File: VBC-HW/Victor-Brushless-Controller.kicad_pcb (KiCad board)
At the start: 2 copper layers, 85 parts, among them J1 i2c QWIIC, P1 PVDD, P2 GND, Q1 TPH4R008NH, Q2 TPH4R008NH, Q3 TPH4R008NH, Q4 TPH4R008NH, Q5 TPH4R008NH, Q6 TPH4R008NH, SW1 SW_SPST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

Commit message: Preliminary component placing
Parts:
- J1: value i2c QWIIC -> i2c/UART; moved to B.Cu
- JP1: value SolderJumper -> 3V3
- P1: value PVDD -> V+
- PA1: value Phase -> A
- PB1: value Phase -> B; moved to B.Cu
- PC1: value Phase -> C
- SW1: value SW_SPST -> BOOT
- SW2: value SW_SPST -> RESET
- U6: value External SPI -> SPI; moved to B.Cu
- U7: moved to B.Cu
- moved C31 113.7 mm to (191.2, 102.0), turned to 90 degrees
- moved C26 113.7 mm to (191.2, 97.0), turned to 90 degrees
- moved PC1 106.4 mm to (192.8, 114.2)
- moved D2 105.7 mm to (194.0, 99.5), turned to 90 degrees
- moved JP1 104.9 mm to (169.7, 74.5)
- moved U2 104.8 mm to (185.0, 81.8)
- moved U5 101.1 mm to (199.5, 106.0), turned to 90 degrees
- moved R1 98.2 mm to (188.0, 101.0), turned to 90 degrees
- moved D1 96.8 mm to (164.5, 76.5), turned to -90 degrees
- moved Q1 95.4 mm to (166.0, 110.0), turned to 180 degrees
- moved PB1 94.7 mm to (177.0, 114.2), turned to 180 degrees
- moved Q2 94.4 mm to (171.5, 108.6)
- moved C30 93.6 mm to (197.0, 107.0), turned to 90 degrees
- moved Q3 93.6 mm to (177.0, 108.6)
- moved R2 93.6 mm to (183.5, 101.0), turned to -90 degrees
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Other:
- board outline added: 44 x 44 mm

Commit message: PCB starting to take shape
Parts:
- D1: value B230A-13-F -> SMA_L4.4-W2.6-LS5.0-RD
- moved C13 61.4 mm to (200.0, 94.2), turned to -90 degrees
- moved R10 57.0 mm to (198.5, 94.0), turned to -90 degrees
- moved R9 56.1 mm to (197.0, 94.0), turned to 90 degrees
- moved R11 53.5 mm to (195.5, 94.0), turned to -90 degrees
- moved C10 10.4 mm to (131.5, 108.5)
- moved LED1 1.80 mm to (153.0, 89.5)
- moved P2 1.50 mm to (198.5, 98.0)
- moved D2 1.00 mm to (194.0, 100.5)
- moved P1 1.00 mm to (198.5, 103.0)
- moved U5 1.00 mm to (199.5, 107.0)
- moved C4 0.50 mm to (158.5, 98.5)
- moved H1 0.50 mm to (197.0, 91.0)
- moved H2 0.50 mm to (197.0, 80.7)
- moved H3 0.50 mm to (199.5, 80.7)

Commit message: Updated PCB and code
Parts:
- C24, C32, C33, C34, C35, C36, C37, C38, C39: moved to B.Cu
- LED1: value Red -> nFault
- LED2: value Blue -> VD
- LED3: value Yellow -> IO15
- moved C38 61.8 mm to (194.2, 98.0), turned to -90 degrees
- moved C37 60.1 mm to (191.2, 98.0), turned to -90 degrees
- moved C36 58.1 mm to (194.0, 103.0), turned to -90 degrees
- moved C39 55.5 mm to (191.5, 103.0), turned to -90 degrees
- moved C24 53.3 mm to (179.2, 103.0), turned to 90 degrees
- moved LED2 50.9 mm to (193.2, 92.0)
- moved R8 49.4 mm to (189.5, 93.2)
- moved R15 49.0 mm to (193.2, 94.2)
- moved C27 48.0 mm to (178.5, 102.5), turned to 90 degrees
- moved C20 47.6 mm to (172.2, 81.8)
- moved C23 47.2 mm to (173.0, 102.5), turned to 90 degrees
- moved R4 46.7 mm to (183.5, 93.2)
- moved C25 46.5 mm to (175.8, 102.5), turned to 90 degrees
- moved C32 46.0 mm to (177.0, 103.0), turned to 90 degrees
- moved C22 44.9 mm to (170.2, 102.5), turned to 90 degrees
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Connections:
- U2 pad 23: IO15 -> IO 15

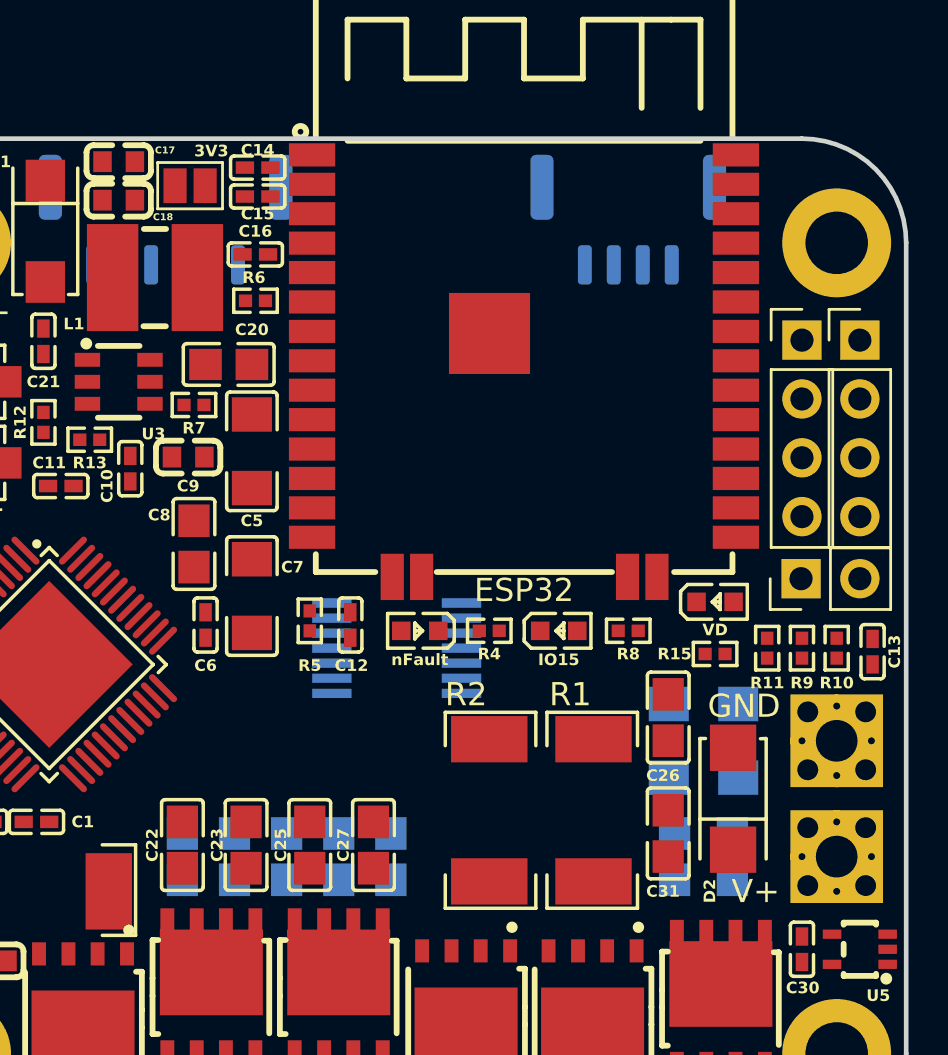
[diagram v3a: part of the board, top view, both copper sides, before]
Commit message: Updates connections in board
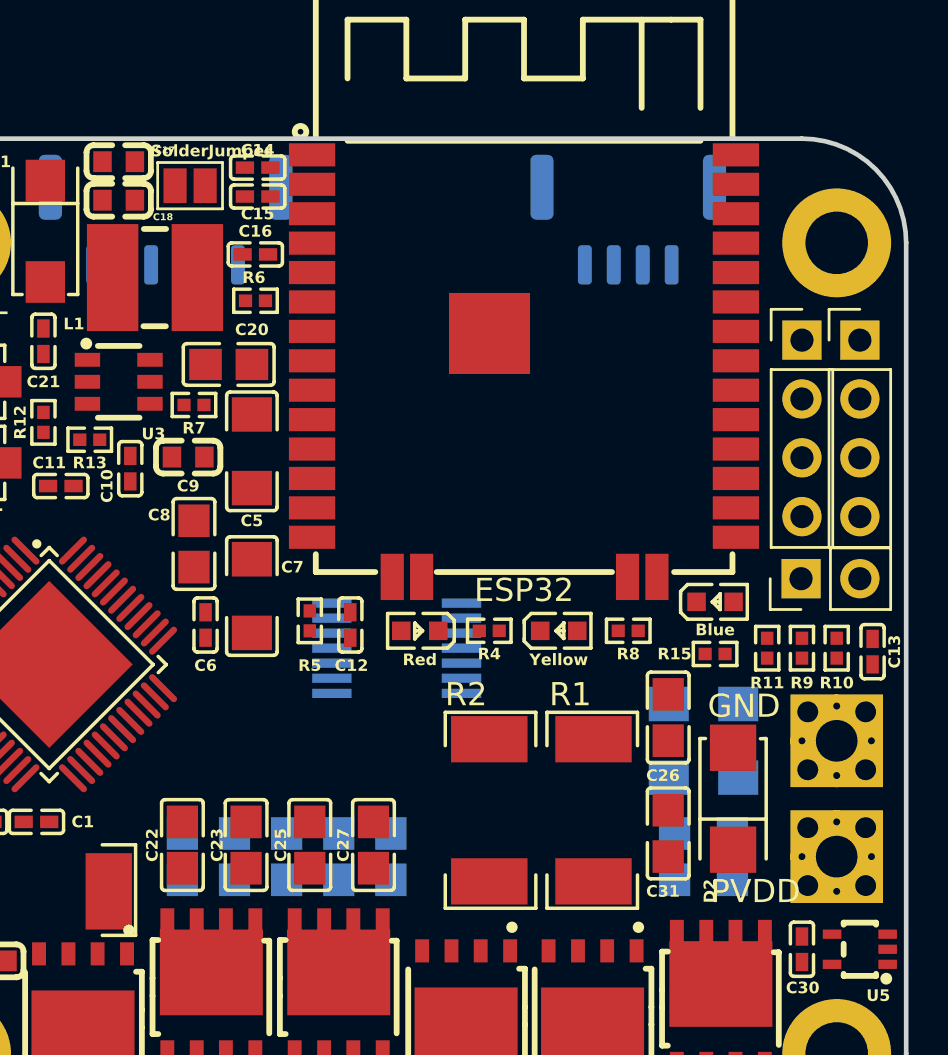
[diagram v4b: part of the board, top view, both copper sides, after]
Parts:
- D1: value SMA_L4.4-W2.6-LS5.0-RD -> B230A-13-F
- J1: value i2c/UART -> i2c QWIIC
- JP1: value 3V3 -> SolderJumper
- LED1: value nFault -> Red
- LED2: value VD -> Blue
- LED3: value IO15 -> Yellow
- P1: value V+ -> PVDD
- U6: value SPI -> External SPI
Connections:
- net IO 15 renamed IO15
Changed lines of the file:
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@@
 	(net 26 "Net-(LED1-K)")
 	(net 27 "Net-(LED2-A)")
-	(net 28 "IO 15")
+	(net 28 "IO15")
 	(net 29 "Net-(LED3-K)")
 	(net 30 "/PA")
@@
 			)
 		)
-		(property "Value" "IO15"
+		(property "Value" "Yellow"
 			(at 0 1.25 0)
 			(layer "F.SilkS")
@@
 			(size 0.8 0.8)
 			(layers "F.Cu" "F.Paste" "F.Mask")
-			(net 28 "IO 15")
+			(net 28 "IO15")
 			(pinfunction "A")
 			(pintype "passive")
@@
 		(at 178.5 102.5 90)
 		(property "Reference" "C27"
-			(at 0 -1.3 270)
+			(at 0 -1.3 -90)
 			(layer "F.SilkS")
 			(effects
@@
 		)
 		(property "Value" "10uF"
-			(at 0 4 270)
+			(at 0 4 -90)
 			(layer "F.Fab")
 			(hide yes)
@@
 			)
 		)
+		(property ki_fp_filters "C_*")
+		(sheetname "Root")
+		(sheetfile "Victor-Brushless-Controller.kicad_sch")
 		(attr smd)
 		(fp_line
@@
 		(at 173 102.5 90)
 		(property "Reference" "C23"
-			(at 0 -1.25 270)
+			(at 0 -1.25 -90)
 			(layer "F.SilkS")
 			(effects
@@
 		)
 		(property "Value" "10uF"
-			(at 0 4 270)
+			(at 0 4 -90)
 			(layer "F.Fab")
 			(hide yes)
@@
 			)
 		)
-		(property "Value" "nFault"
+		(property "Value" "Red"
 			(at 0 -1.25 180)
 			(layer "F.SilkS")
@@
 		(at 175.75 102.5 90)
 		(property "Reference" "C25"
-			(at 0 -1.25 270)
+			(at 0 -1.25 -90)
 			(layer "F.SilkS")
 			(effects
@@
 		)
 		(property "Value" "10uF"
-			(at 0 4 270)
+			(at 0 4 -90)
 			(layer "F.Fab")
 			(hide yes)
@@
 			)
 		)
-		(property "Value" "VD"
+		(property "Value" "Blue"
 			(at 0 1.21 0)
 			(layer "F.SilkS")
@@
 			)
 		)
+		(sheetname "Root")
+		(sheetfile "Victor-Brushless-Controller.kicad_sch")
 		(attr smd)
 		(fp_line
@@
 			)
 		)
-		(property "Value" "3V3"
+		(property "Value" "SolderJumper"
 			(at 0.917764 -1.5 0)
 			(layer "F.SilkS")
@@
 			)
 		)
-		(property "Value" "SMA_L4.4-W2.6-LS5.0-RD"
+		(property "Value" "B230A-13-F"
 			(at 0 4 -90)
 			(layer "F.Fab")
@@
 			)
 		)
+		(sheetname "Root")
+		(sheetfile "Victor-Brushless-Controller.kicad_sch")
 		(attr smd)
 		(fp_line
@@
 			)
 		)
-		(property "Value" "V+"
+		(property "Value" "PVDD"
 			(at -3.5 1.5 0)
 			(unlocked yes)
@@
 			)
 		)
+		(sheetname "Root")
+		(sheetfile "Victor-Brushless-Controller.kicad_sch")
 		(attr smd)
 		(fp_line
@@
 			)
 		)
+		(property ki_fp_filters "C_*")
+		(sheetname "Root")
+		(sheetfile "Victor-Brushless-Controller.kicad_sch")
 		(attr smd)
 		(fp_line
@@
 		(at 170.25 102.5 90)
 		(property "Reference" "C22"
-			(at 0 -1.3 270)
+			(at 0 -1.3 -90)
 			(layer "F.SilkS")
 			(effects
@@
 		)
 		(property "Value" "10uF"
-			(at 0 4 270)
+			(at 0 4 -90)
 			(layer "F.Fab")
 			(hide yes)
@@
 			)
 		)
+		(sheetname "Root")
+		(sheetfile "Victor-Brushless-Controller.kicad_sch")
 		(attr smd)
 		(fp_line
@@
 			)
 		)
+		(property ki_fp_filters "Choke_* *Coil* Inductor_* L_*")
+		(sheetname "Root")
+		(sheetfile "Victor-Brushless-Controller.kicad_sch")
 		(attr smd)
 		(fp_line
@@
 			)
 		)
+		(property ki_fp_filters "C_*")
+		(sheetname "Root")
+		(sheetfile "Victor-Brushless-Controller.kicad_sch")
 		(attr smd)
 		(fp_line
@@
 			)
 		)
+		(sheetname "Root")
+		(sheetfile "Victor-Brushless-Controller.kicad_sch")
 		(attr smd)
 		(fp_line
@@
 			(size 2 1)
 			(layers "F.Cu" "F.Paste" "F.Mask")
-			(net 28 "IO 15")
+			(net 28 "IO15")
 			(pinfunction "IO15")
 			(pintype "unspecified")
@@
 			)
 		)
+		(sheetname "Root")
+		(sheetfile "Victor-Brushless-Controller.kicad_sch")
 		(attr smd)
 		(fp_line
@@
 		)
 		(property "Value" "10uF"
-			(at 0 -4 270)
+			(at 0 -4 -90)
 			(layer "B.Fab")
 			(hide yes)
@@
 		)
 		(property "Value" "10uF"
-			(at 0 -4 270)
+			(at 0 -4 -90)
 			(layer "B.Fab")
 			(hide yes)
@@
 		)
 		(property "Value" "10uF"
-			(at 0 -4 270)
+			(at 0 -4 -90)
 			(layer "B.Fab")
 			(hide yes)
@@
 			)
 		)
-		(property "Value" "SPI"
+		(property "Value" "External SPI"
 			(at -6.975 0.5 180)
 			(layer "B.SilkS")
@@
 			)
 		)
-		(property "Value" "i2c/UART"
+		(property "Value" "i2c QWIIC"
 			(at 6.5 0.5 180)
 			(layer "B.SilkS")
@@
 		)
 		(property "Value" "10uF"
-			(at 0 -4 270)
+			(at 0 -4 -90)
 			(layer "B.Fab")
 			(hide yes)
@@
 		)
 		(property "Value" "10uF"
-			(at 0 -4 270)
+			(at 0 -4 -90)
 			(layer "B.Fab")
 			(hide yes)

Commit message: Starting added traces to board
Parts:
- removed REF**: MountingHole_2.7mm_M2.5_DIN965_Pad, MountingHole:MountingHole_2.7mm_M2.5_DIN965_Pad
- added ?: , , F.Cu at (160.5, 111.5)
- JP1: value SolderJumper -> 3V3
- P1: value PVDD -> V+
- moved Q6 27.5 mm to (166.0, 110.0), turned to 180 degrees
- moved PA1 22.2 mm to (193.0, 114.5)
- moved PC1 22.2 mm to (170.8, 114.5)
- moved Q1 21.9 mm to (187.9, 109.9)
- moved Q2 21.9 mm to (193.4, 108.9)
- moved Q5 16.5 mm to (171.5, 108.9), turned to 0 degrees
- moved C16 2.25 mm to (173.4, 79.2)
- moved C10 1.98 mm to (167.3, 88.1), turned to 0 degrees
- moved C6 1.80 mm to (171.2, 94.8), turned to -90 degrees
- moved R6 1.75 mm to (173.4, 77.2)
- moved C8 1.23 mm to (171.0, 90.7)
- moved C11 1.17 mm to (164.6, 88.1), turned to 180 degrees
- moved C9 1.09 mm to (170.2, 86.8)
- moved C4 0.92 mm to (158.3, 97.6), turned to -90 degrees
- moved R7 0.90 mm to (170.8, 84.4)
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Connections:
- H2 pad 1: BOOT IO0 -> TX0
- H2 pad 2: RESET EN -> RX0
- H2 pad 3: RX0 -> RESET EN
- H2 pad 4: TX0 -> BOOT IO0
- U2 pad 39: unconnected-(U2-P_GND-Pad39) -> GND
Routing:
- net GND: track 0.00 -> 76.5 mm
- net /GHB: track 0.00 -> 25.6 mm
- net IO22: track 0.00 -> 22.5 mm
- net IO21: track 0.00 -> 21.2 mm
- net /GHC: track 0.00 -> 20.2 mm
- net VCC: track 0.00 -> 17.8 mm
- net /PC: track 0.00 -> 14.9 mm
- net /SLC: track 0.00 -> 10.9 mm
- net /GLC: track 0.00 -> 8.91 mm
- net 3V3A: track 0.00 -> 8.29 mm
- net Net-(U1-VDRAIN): track 0.00 -> 8.20 mm
- net RESET EN: track 0.00 -> 6.91 mm
- net Net-(U1-CP1L): track 0.00 -> 6.69 mm
- net Net-(U1-CP1H): track 0.00 -> 5.67 mm
- net BOOT IO0: track 0.00 -> 5.63 mm
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
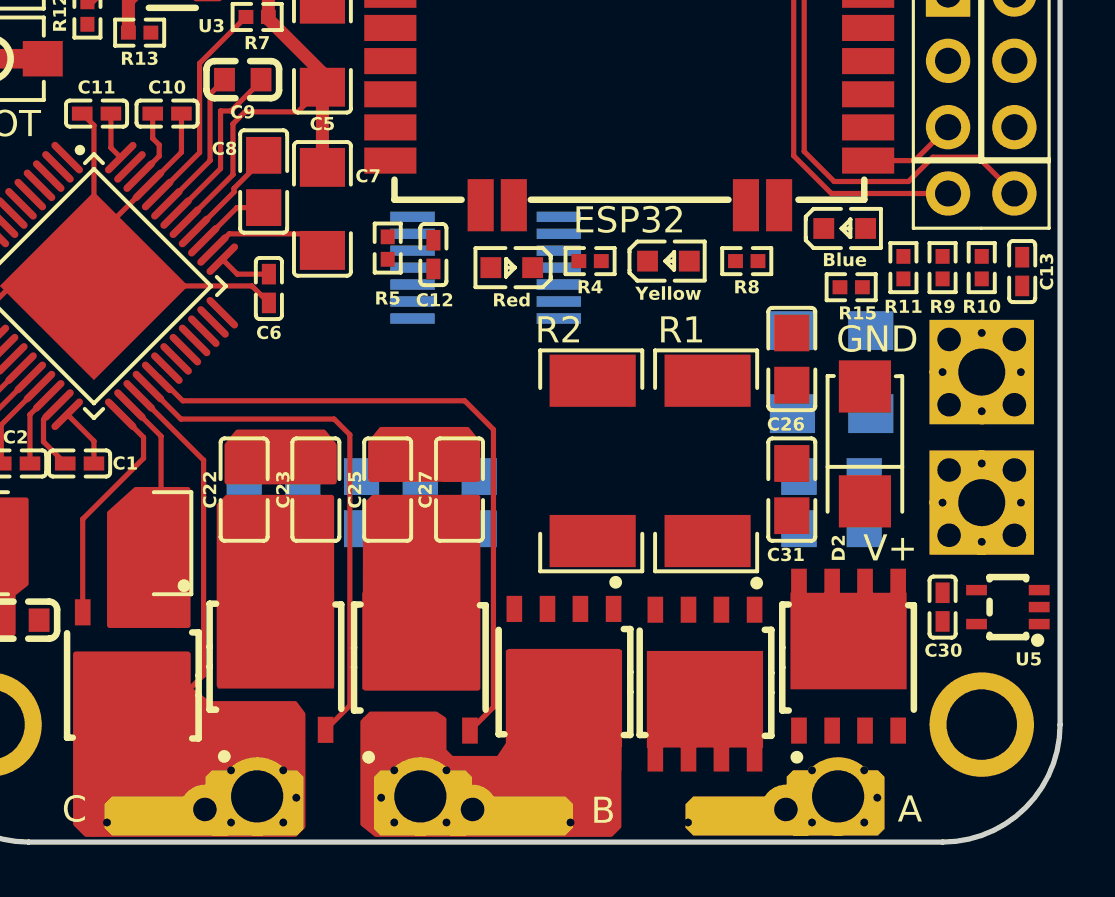
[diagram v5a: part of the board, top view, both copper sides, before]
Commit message: Finished top layer connections
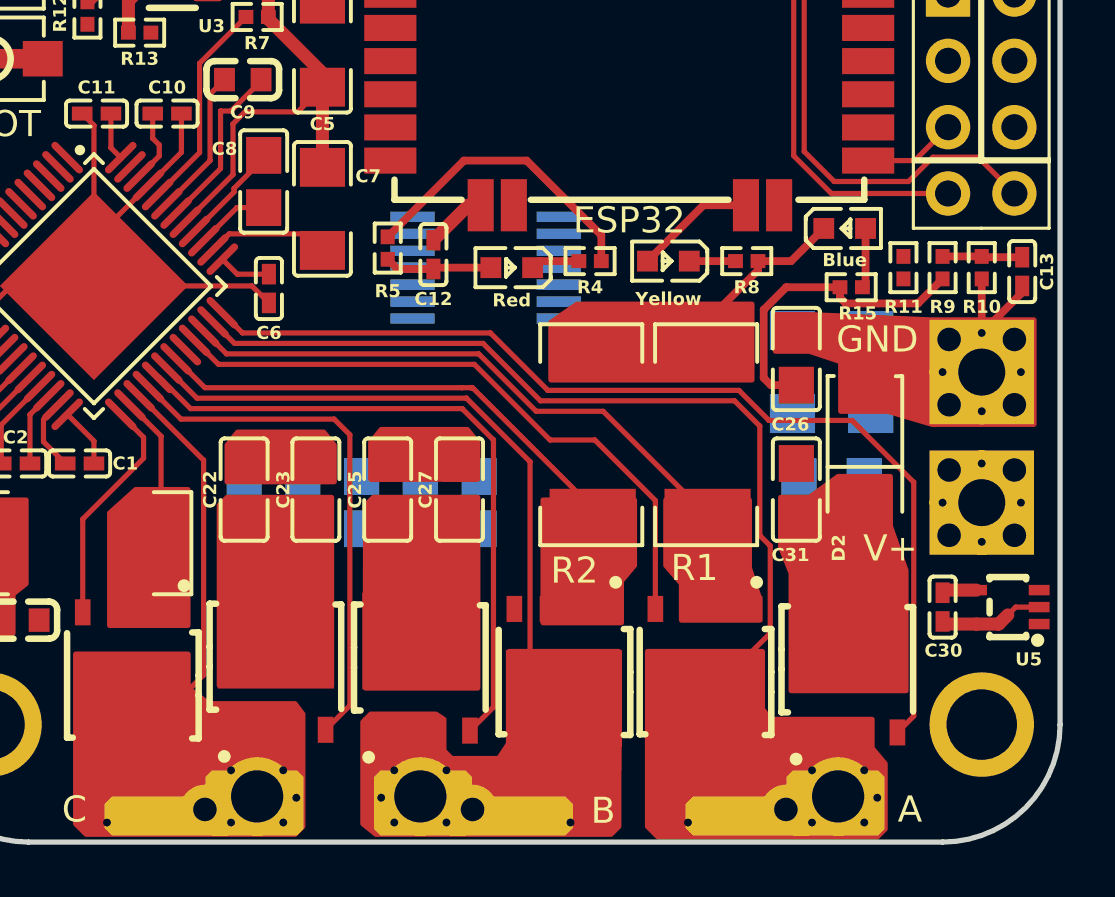
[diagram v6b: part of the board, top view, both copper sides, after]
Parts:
- moved Q2 5.58 mm to (187.9, 109.9), turned to 180 degrees
- moved Q1 5.54 mm to (193.4, 109.0), turned to 0 degrees
- moved R1 1.00 mm to (188.0, 100.4)
- moved R2 1.00 mm to (183.6, 100.4)
- moved C26 0.17 mm to (191.4, 97.5)
- moved C31 0.17 mm to (191.4, 102.5)
- turned C12 to -90 degrees
- turned LED3 to 180 degrees
- turned R5 to 90 degrees
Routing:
- net /GHA: track 0.00 -> 39.0 mm
- net /PA: track 0.00 -> 34.2 mm
- net /PB: track 0.00 -> 25.0 mm
- net /GLA: track 0.00 -> 24.3 mm
- net /SLA: track 2.81 -> 25.4 mm
- net /SLB: track 3.55 -> 23.1 mm
- net GND: track 76.5 -> 94.8 mm
- net VCC: track 17.8 -> 29.9 mm
- net nFault IO4: track 0.00 -> 11.6 mm
- net 3V3A: track 8.29 -> 13.8 mm
- net IO15: track 0.00 -> 4.66 mm
- net Vbus IO33: track 0.00 -> 3.06 mm
- net Net-(LED2-A): track 0.00 -> 2.30 mm
- net Net-(LED1-K): track 0.00 -> 1.87 mm
- net Net-(LED3-K): track 0.00 -> 1.77 mm
